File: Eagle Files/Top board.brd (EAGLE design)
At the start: 254 x 1272.5 mm, 3 parts, among them J1 MINI-USB-5P-3400030P1, U1 CN3065-1320040P1

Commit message: Tweak board
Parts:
- removed J2: (no value), Connector:2P-SMD-2.0-90D
- moved J1 32.6 mm to (35.0, 12.1)
- moved U1 13.6 mm to (32.0, 4.24)
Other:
- board size 254 x 1272.5 mm -> 21.8 x 20.3 mm
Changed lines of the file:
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@@
 <setting verticaltext="up"/>
 </settings>
-<grid distance="1" unitdist="mil" unit="mil" style="lines" multiple="1" display="no" altdistance="0.025" altunitdist="inch" altunit="inch"/>
+<grid distance="5" unitdist="mil" unit="mil" style="lines" multiple="1" display="no" altdistance="1" altunitdist="mil" altunit="mil"/>
 <layers>
 <layer number="1" name="Top" color="4" fill="1" visible="yes" active="yes"/>
@@
 <board>
 <plain>
-<wire x1="0" y1="0" x2="100" y2="0" width="0" layer="20"/>
-<wire x1="100" y1="0" x2="100" y2="80" width="0" layer="20"/>
-<wire x1="100" y1="80" x2="0" y2="80" width="0" layer="20"/>
-<wire x1="0" y1="80" x2="0" y2="0" width="0" layer="20"/>
-<wire x1="95.25" y1="1272.54" x2="95.25" y2="256.54" width="0.0254" layer="20"/>
-<wire x1="254" y1="1272.54" x2="95.25" y2="1272.54" width="0.0254" layer="20"/>
-<wire x1="95.25" y1="256.54" x2="254" y2="256.54" width="0.0254" layer="20"/>
+<wire x1="37.211" y1="0" x2="45.085" y2="7.874" width="0" layer="20" curve="90"/>
+<wire x1="45.085" y1="7.874" x2="45.085" y2="12.446" width="0" layer="20"/>
+<wire x1="45.085" y1="12.446" x2="37.211" y2="20.32" width="0" layer="20" curve="90"/>
+<wire x1="37.211" y1="20.32" x2="25.781" y2="20.32" width="0" layer="20"/>
+<wire x1="25.781" y1="4.064" x2="23.241" y2="2.794" width="0" layer="20"/>
+<wire x1="23.241" y1="2.794" x2="23.241" y2="0" width="0" layer="20"/>
+<wire x1="23.241" y1="0" x2="37.211" y2="0" width="0" layer="20"/>
+<wire x1="25.781" y1="4.064" x2="25.781" y2="20.32" width="0" layer="20"/>
 </plain>
 <attributes>
@@
 </autorouter>
 <elements>
-<element name="J1" library="Connector" package="MINI-B-5P-SMD" value="MINI-USB-5P-3400030P1" x="31.75" y="44.45"/>
-<element name="J2" library="Connector" package="2P-SMD-2.0-90D" value="" x="50.8" y="29.21"/>
-<element name="U1" library="IC" package="DFN8" value="CN3065-1320040P1" x="33.02" y="17.78"/>
+<element name="J1" library="Connector" package="MINI-B-5P-SMD" value="MINI-USB-5P-3400030P1" x="35.0266" y="12.065"/>
+<element name="U1" library="IC" package="DFN8" value="CN3065-1320040P1" x="32.0294" y="4.2418"/>
 </elements>
 <signals>

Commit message: Tweaks
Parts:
- added RD2007: RD2007, radiationbean:RD2007
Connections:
- new net GND: RD2007.GND
- new net VCC: RD2007.VCC
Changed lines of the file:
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@@
 <layer number="45" name="Holes" color="7" fill="1" visible="no" active="yes"/>
 <layer number="46" name="Milling" color="3" fill="1" visible="no" active="yes"/>
-<layer number="47" name="Measures" color="7" fill="1" visible="no" active="yes"/>
+<layer number="47" name="Measures" color="7" fill="1" visible="yes" active="yes"/>
 <layer number="48" name="Document" color="7" fill="1" visible="yes" active="yes"/>
 <layer number="49" name="Reference" color="7" fill="1" visible="yes" active="yes"/>
@@
 <wire x1="23.241" y1="0" x2="37.211" y2="0" width="0" layer="20"/>
 <wire x1="25.781" y1="4.064" x2="25.781" y2="20.32" width="0" layer="20"/>
+<dimension x1="19.558" y1="2.286" x2="19.558" y2="18.288" x3="17.861753125" y3="10.287" textsize="1.778" layer="47" unit="mil"/>
 </plain>
 <attributes>
@@
 <element name="J1" library="Connector" package="MINI-B-5P-SMD" value="MINI-USB-5P-3400030P1" x="35.0266" y="12.065"/>
 <element name="U1" library="IC" package="DFN8" value="CN3065-1320040P1" x="32.0294" y="4.2418"/>
+<element name="RD2007" library="radiationbean" package="RD2007" value="RD2007" x="47.4472" y="3.429" rot="MR0"/>
 </elements>
 <signals>
+<signal name="GND">
+<contactref element="RD2007" pad="GND"/>
+</signal>
+<signal name="VCC">
+<contactref element="RD2007" pad="VCC"/>
+</signal>
 </signals>
 </board>
 </drawing>
+<compatibility>
+<note version="6.3" minversion="6.2.2" severity="warning">
+Since Version 6.2.2 text objects can contain more than one line,
+which will not be processed correctly with this version.
+</note>
+</compatibility>
 </eagle>

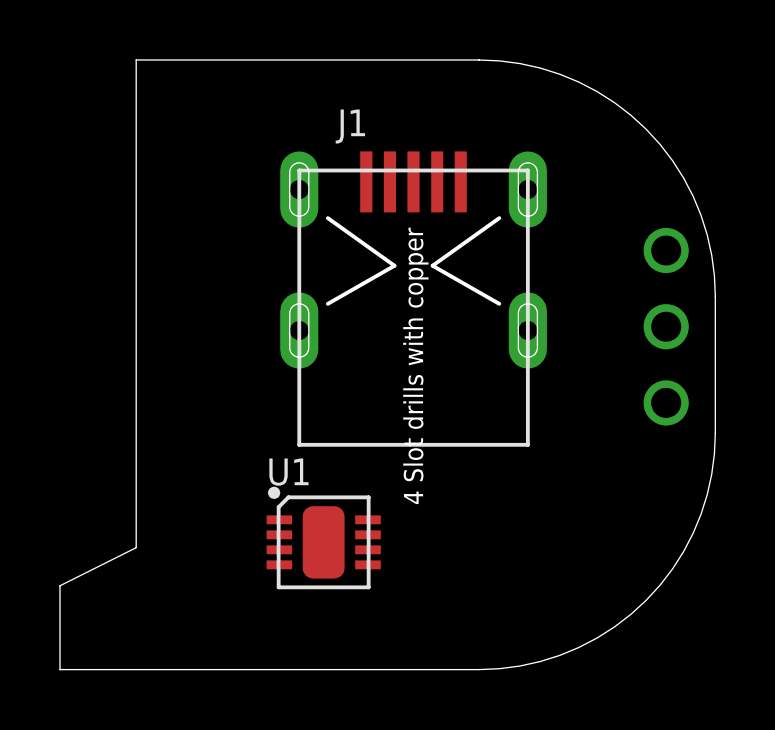
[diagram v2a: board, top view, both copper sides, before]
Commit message: Renamed Eagle files.
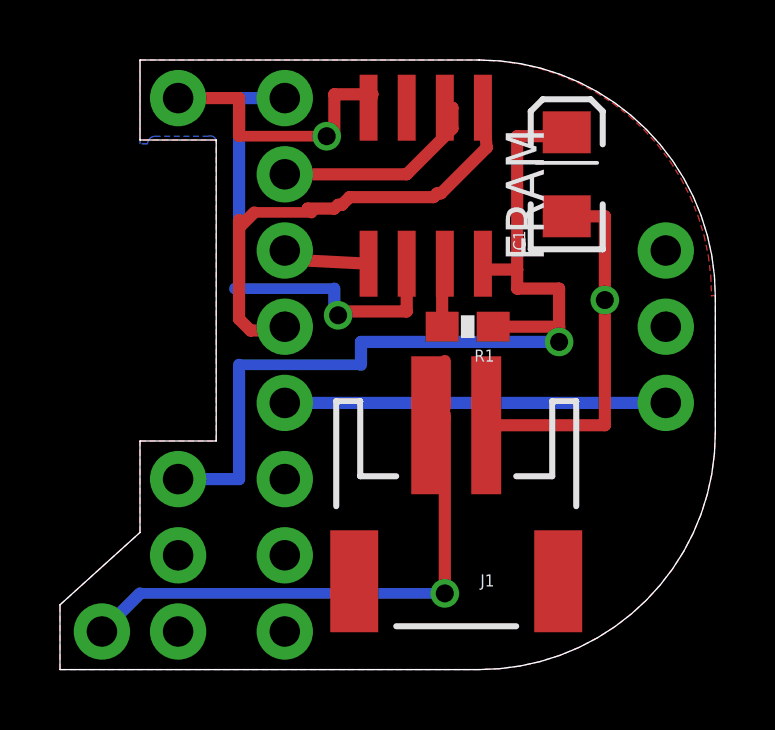
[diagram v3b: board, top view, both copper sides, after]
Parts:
- removed RD2007: RD2007, radiationbean:RD2007
- removed U1: CN3065-1320040P1, IC:DFN8
- added 0, 1, 2, 3, 4, 4V, 5, A0, A1, BAT, DATA, GND@1, GND@2, GND@3, RESET, VCC: PROTO_POINT, BLEduino Bean:1X01
- added C1: 10uF, SparkFun-Capacitors:EIA3216
- added FRAM: MB85RS64V, radiationbean:SO08
- added R1: 10K, SparkFun-Resistors:0603-RES
- J1: value MINI-USB-5P-3400030P1 -> (none); device Connector:MINI-B-5P-SMD -> SparkFun-Connectors:JST-2-SMD
- moved J1 7.75 mm to (36.4, 4.45), turned to 180 degrees
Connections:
- new net 4V: 4V.1
- new net CLK: 5.1, FRAM.SCK
- new net CS: 2.1, FRAM.CS
- new net DATA: 1.1, DATA.1
- new net HOLD: FRAM.HOLD, R1.2
- new net MISO: 4.1, FRAM.SO
- new net MOSI: 3.1, FRAM.SI
- new net N$4: RESET.1
- new net N$5: A0.1
- new net N$6: A1.1
- new net N$7: 0.1
- new net VBAT: BAT.1, J1.2
- new net WP: FRAM.WP
- net GND: now also C1.C, FRAM.GND, GND@1.1, GND@2.1, GND@3.1, J1.1; no longer RD2007.GND
- net VCC: now also C1.A, FRAM.VDD, R1.1, VCC.1; no longer RD2007.VCC
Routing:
- net VCC: track 0.00 -> 31.2 mm, vias 0 -> 1
- net GND: track 0.00 -> 21.8 mm, vias 0 -> 2
- net VBAT: track 0.00 -> 21.8 mm, vias 0 -> 1
- net CLK: track 0.00 -> 16.5 mm, vias 0 -> 1
- net CS: track 0.00 -> 16.0 mm
- net DATA: track 0.00 -> 12.7 mm
- net MISO: track 0.00 -> 7.17 mm
- net MOSI: track 0.00 -> 2.93 mm
- net HOLD: track 0.00 -> 2.14 mm
- added copper zone on layer 1, net GND
- added copper zone on layer 16, net GND
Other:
- outline, holes or cut-outs redrawn
- board text added: "Avoid placing copper in antenna keepout"
- board text added: "Bean Revision E"
- board text added: "Bottom Silk: bArt"
- board text added: "Copper Weight: 1oz"
- board text added: "Corner mill radius: 0.32""
- board text added: "Finish: ENIG"
- board text added: "Finished Thickness: 0.062""
- board text added: "Layers: 2"
- board text added: "Material: FR4"
- board text added: "Min Annular Ring: 0.006""
- board text added: "Min Drill: 0.008""
- board text added: "Min Spacing: 0.005""
- board text added: "Min Trace: 0.007""
- board text added: "P/N: PTD1013012E"
- board text added: "Rectangular Dimensions: 1.775" x 0.8" (45.09mm x 20.32mm)"
- board text added: "Rev E"
- board text added: "Silkscreen Color: Black"
- board text added: "Silkscreen: Top and Bottom"
- board text added: "Soldermask Color: 85% white 10% green 5% blue"
- board text added: "Soldermask: Top and bottom"
- board text added: "Top Board"
- board text added: "Top Silk: tPlace tArt"
- board text added: "ck@"
- board text added: "punchthrough.com"
- board text added: "ray@"
- board text added: "v0.1"

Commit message: v0.2
Switched to 32KB I2C Fram.
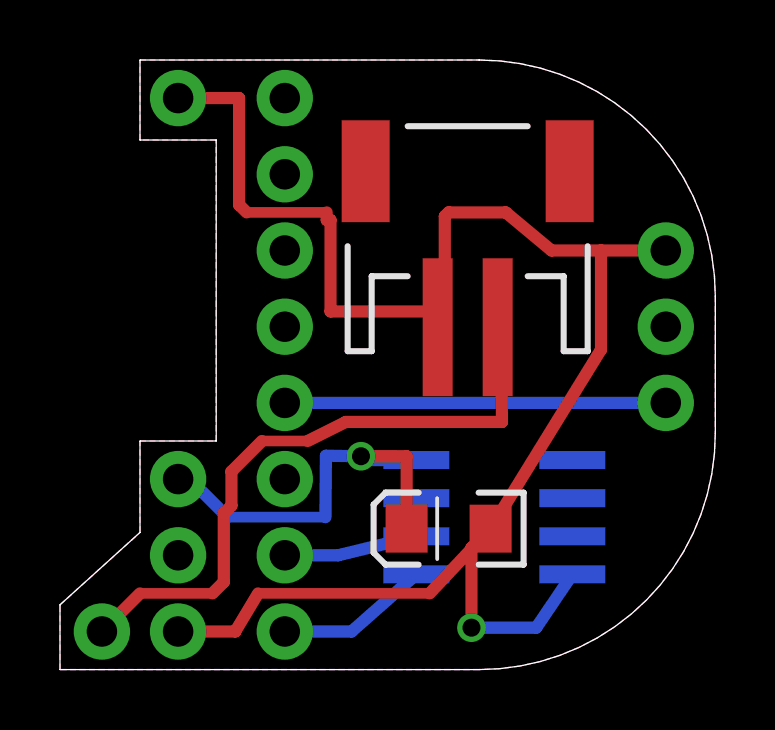
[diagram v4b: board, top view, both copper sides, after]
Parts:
- removed R1: 10K, SparkFun-Resistors:0603-RES
- FRAM: value MB85RS64V -> MB85RC256V
- moved C1 12.4 mm to (36.2, 4.70), turned to 180 degrees
- moved FRAM 11.3 mm to (37.7, 5.08), flipped to the bottom, turned to 270 degrees
- moved J1 10.7 mm to (36.8, 15.1), turned to 0 degrees
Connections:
- removed net HOLD: FRAM.HOLD, R1.2
- removed net N$5: A0.1
- removed net N$6: A1.1
- new net A0: FRAM.A0
- new net A1: FRAM.A1
- new net A2: FRAM.A2
- new net SCL: A1.1, FRAM.SCL
- new net SDA: A0.1, FRAM.SDA
- net CLK: no longer FRAM.SCK
- net CS: no longer FRAM.CS
- net MISO: no longer FRAM.SO
- net MOSI: no longer FRAM.SI
- net VCC: no longer R1.1
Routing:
- net GND: track 21.8 -> 57.9 mm, vias 2 -> 1
- net CLK: track 16.5 -> 0.00 mm, vias 1 -> 0
- net CS: track 16.0 -> 0.00 mm
- net VCC: track 31.2 -> 15.8 mm
- net MISO: track 7.17 -> 0.00 mm
- net SDA: track 0.00 -> 5.11 mm
- net SCL: track 0.00 -> 4.46 mm
- net MOSI: track 2.93 -> 0.00 mm
- net HOLD: track 2.14 -> 0.00 mm
- net VBAT: track 21.8 -> 21.3 mm, vias 1 -> 0
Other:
- board text added: "0"
- board text added: "1"
- board text added: "CS"
- board text added: "G"
- board text added: "MI"
- board text added: "MO"
- board text added: "RST"
- board text added: "SCK"
- board text added: "SCL"
- board text added: "SDA"
- board text added: "VBAT"
- board text added: "VCC"
- board text added: "v0.2"
- board text removed: "v0.1"
